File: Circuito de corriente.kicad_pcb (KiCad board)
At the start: 2 copper layers, 150 x 120 mm, 110 parts, among them J1 SALIDAS, J2 ENTRADAS, J3 +12V2, J4 +3V3, J5 +/- 5V, J6 +/- 12V, J7 INPUT_CEDCp, K1 JJM1-12V, K2 JJM1-12V, K3 JJM1-12V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

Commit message: Added 3D model
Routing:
- added copper zone on F.Cu, net GND
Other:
- board text added: "4 PINES DE ENTRADAS"

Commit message: Gerbers files generated
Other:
- board text removed: "4 PINES DE ENTRADAS"
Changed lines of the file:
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@@
       (outputformat 1)
       (mirror false)
-      (drillshape 1)
+      (drillshape 0)
       (scaleselection 1)
-      (outputdirectory "")
+      (outputdirectory "Gerbers/")
     )
   )
@@
     (effects (font (size 1 1) (thickness 0.25)))
   )
-  (gr_text "4 PINES DE ENTRADAS" (at 228.6 67.5) (layer "F.SilkS")
-    (effects (font (size 1 1) (thickness 0.15)))
-  )
   (dimension (type aligned) (layer "Margin")

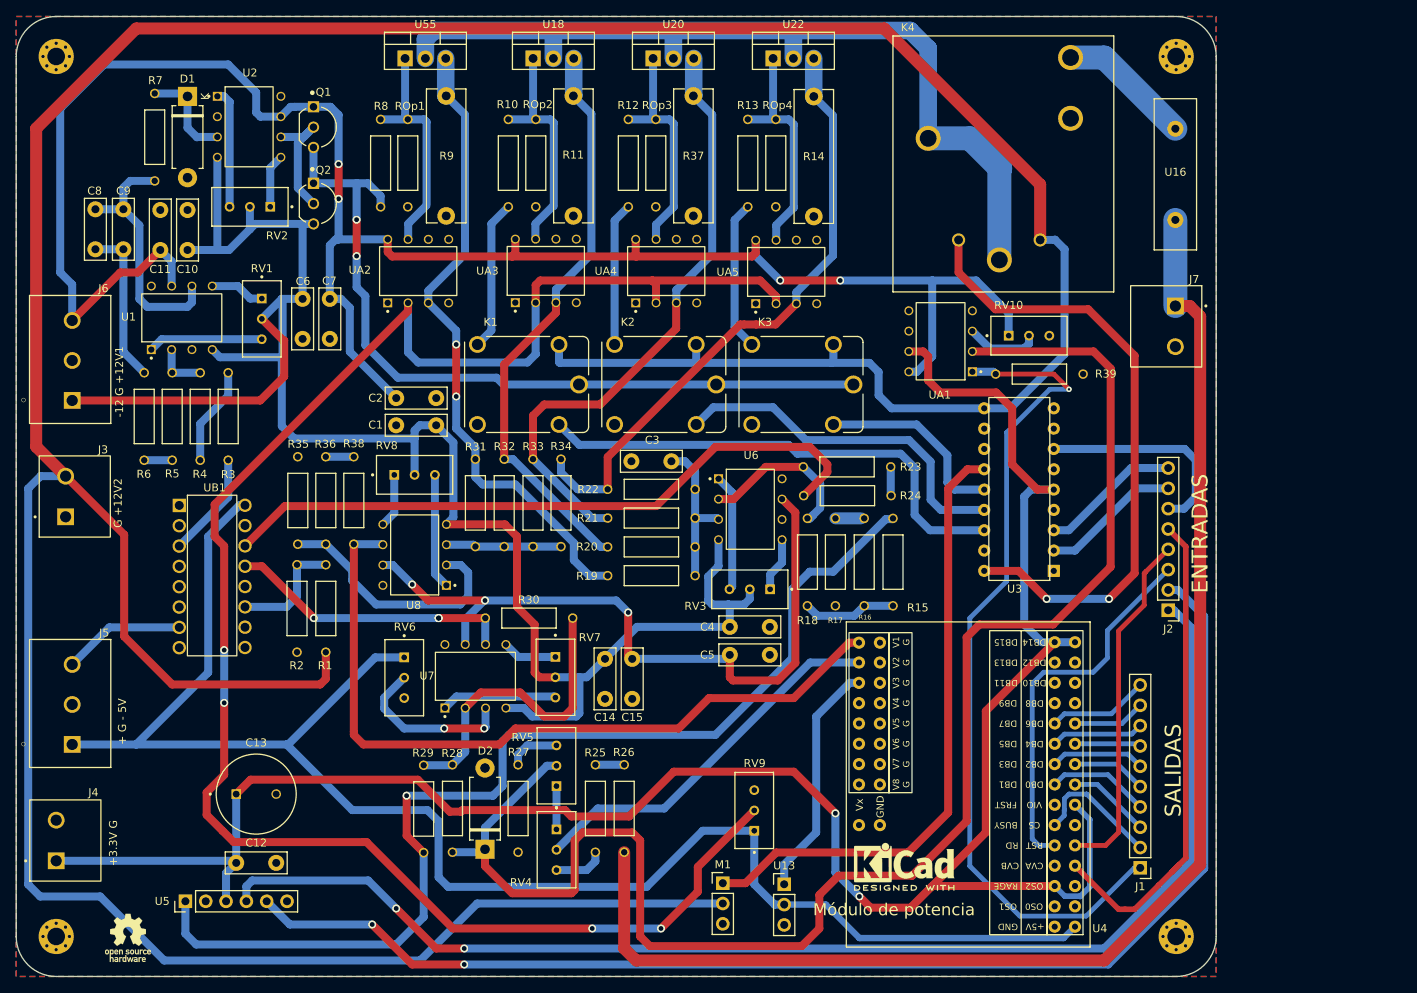
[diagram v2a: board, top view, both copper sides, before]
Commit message: Reorder conection with control module
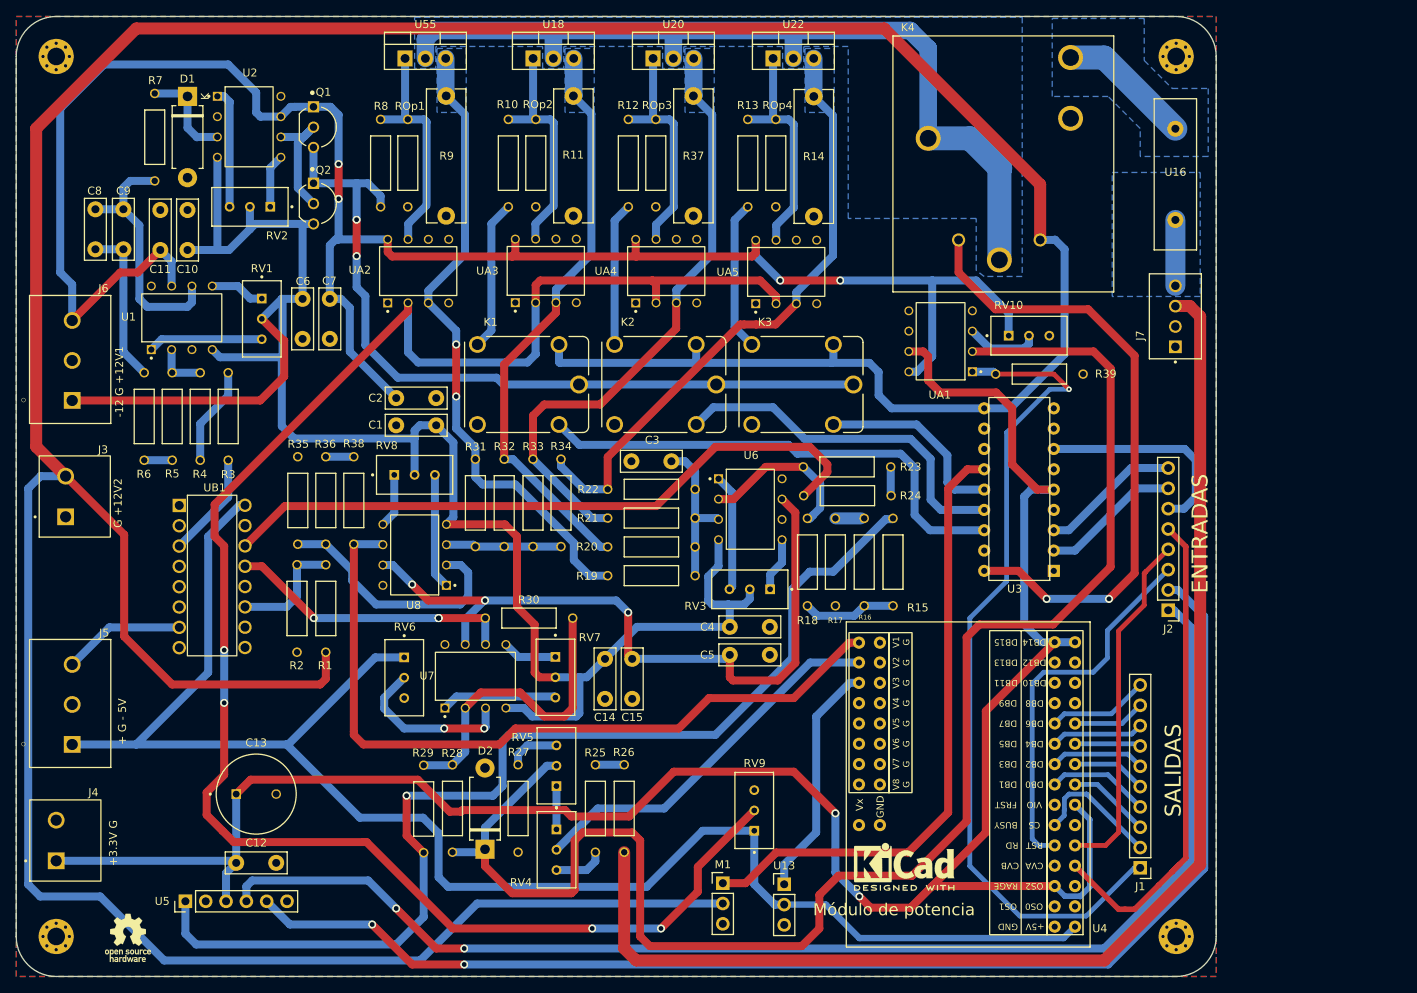
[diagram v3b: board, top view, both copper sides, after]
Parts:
- J7: footprint CEDCp:Bornera_1x2 -> CEDCp:Bornera_1x4
- moved J7 2.56 mm to (210.1, 69.0), turned to 90 degrees
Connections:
- net Net-(K4-PadNC) renamed /Proteccion Sobre Tension (53V)/F_In
- J1 pad 1: /toMicroC_OverVoltageSignal -> /toMicroC_ADC_DB0
- J1 pad 10: /toMicroC_ADC_DB7 -> /toMicroC_ADC_BUSY
- J1 pad 2: /toMicroC_ADC_BUSY -> /toMicroC_ADC_DB1
- J1 pad 3: /toMicroC_ADC_DB0 -> /toMicroC_ADC_DB2
- J1 pad 4: /toMicroC_ADC_DB1 -> /toMicroC_ADC_DB3
- J1 pad 5: /toMicroC_ADC_DB2 -> /toMicroC_ADC_DB4
- J1 pad 6: /toMicroC_ADC_DB3 -> /toMicroC_ADC_DB5
- J1 pad 7: /toMicroC_ADC_DB4 -> /toMicroC_ADC_DB6
- J1 pad 8: /toMicroC_ADC_DB5 -> /toMicroC_ADC_DB7
- J1 pad 9: /toMicroC_ADC_DB6 -> /toMicroC_OverVoltageSignal
- J2 pad 1: /fromMicroC_DACI2C_SDA -> /fromMicroC_ADC_RD
- J2 pad 2: /fromMicroC_DACI2C_SCL -> /fromMicroC_ADC_RST
- J2 pad 3: /fromMicroC_ADC_RD -> /fromMicroC_ADC_CONV
- J2 pad 4: /fromMicroC_ADC_RST -> /fromMicroC_DACI2C_SCL
- J2 pad 5: /fromMicroC_ADC_CONV -> /fromMicroC_DACI2C_SDA
- J7 pad 2: /CEP_Input+ -> GND
- K4 pad NO: unconnected-(K4-PadNO) -> GND
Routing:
- net /fromMicroC_DACI2C_SCL: track 162.8 -> 0.00 mm, vias 2 -> 0
- net /fromMicroC_ADC_RST: track 44.1 -> 206.9 mm, vias 0 -> 2
- net /fromMicroC_DACI2C_SDA: track 161.4 -> 0.00 mm, vias 2 -> 0
- net /fromMicroC_ADC_RD: track 47.5 -> 161.4 mm, vias 0 -> 2
- net /fromMicroC_ADC_CONV: track 62.1 -> 109.6 mm
- net /toMicroC_ADC_BUSY: track 16.3 -> 0.00 mm
- net /toMicroC_ADC_DB7: track 12.7 -> 24.3 mm
- net /toMicroC_ADC_DB2: track 9.31 -> 0.00 mm
- net /toMicroC_OverVoltageSignal: track 105.5 -> 114.6 mm
- net /toMicroC_ADC_DB1: track 12.9 -> 16.3 mm
- net /CEP_Input+: track 172.5 -> 170.0 mm
- net /toMicroC_ADC_DB4: track 8.26 -> 9.31 mm
- net /toMicroC_ADC_DB3: track 11.8 -> 12.9 mm
- net /+5V: track 204.9 -> 204.1 mm
- net /toMicroC_ADC_DB6: track 9.09 -> 8.26 mm
- added copper zone on B.Cu, net /CEP_Input+
- added copper zone on B.Cu, net /CEP_Input+_MOS
- added copper zone on B.Cu, net /Proteccion Sobre Tension (53V)/F_In
- added copper zone on B.Cu, net /V1
- added copper zone on B.Cu, net /V2
- added copper zone on B.Cu, net /V3
- added copper zone on B.Cu, net /V4

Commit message: Gerbers generated again
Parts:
- moved U5 118.1 mm to (199.2, 103.6), turned to -90 degrees
- moved C12 117.4 mm to (209.2, 119.2), turned to 180 degrees
- moved C13 111.6 mm to (206.7, 126.1), turned to 180 degrees
- moved M1 79.3 mm to (209.3, 79.6)
- moved REF** 77.6 mm to (98.7, 138.0)
- moved R29 71.9 mm to (187.6, 134.7), turned to 180 degrees
- moved J1 71.0 mm to (140.6, 105.8), turned to -90 degrees
- moved D2 69.0 mm to (192.7, 127.0), turned to 180 degrees
- moved R28 68.0 mm to (187.6, 131.1), turned to 180 degrees
- moved U13 68.0 mm to (94.2, 124.7)
- moved RV6 65.2 mm to (173.1, 137.2), turned to 0 degrees
- moved RV9 63.8 mm to (94.2, 118.2), turned to 180 degrees
- moved RV4 61.6 mm to (192.7, 118.1), turned to 0 degrees
- moved R27 59.7 mm to (187.6, 122.9), turned to 0 degrees
- moved U4 54.7 mm to (150.1, 114.2), turned to -90 degrees
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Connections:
- J7 pad 3: /CEP_Input+ -> /CEP_Input+_2
- J7 pad 4: /CEP_Input+ -> /CEP_Inpunt+_1
- R25 pad 1: /CEP_Input+ -> /CEP_Input+_2
- U16 pad 1: /CEP_Input+ -> /CEP_Inpunt+_1
- U2 pad 2: unconnected-(U2-Pad2) -> /PushPullOut
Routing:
- net /+12V2: track 487.2 -> 237.2 mm
- net /CEP_Input+: track 170.0 -> 0.00 mm
- net /fromMicroC_ADC_RST: track 206.9 -> 51.4 mm, vias 2 -> 0
- net /fromMicroC_ADC_RD: track 161.4 -> 54.1 mm, vias 2 -> 0
- net /+12V1: track 333.6 -> 401.2 mm, vias 7 -> 2
- net /Error2: track 36.0 -> 101.6 mm, vias 3 -> 1
- net /CEP_Input+_2: track 0.00 -> 63.1 mm
- net /fromDAC_Vref: track 135.3 -> 73.2 mm
- net /fromA6841_toFanEnable: track 77.8 -> 16.5 mm
- net /+3.3V: track 268.4 -> 329.4 mm, vias 2 -> 0
- net /toADC_LoadVoltage: track 47.5 -> 106.4 mm, vias 0 -> 2
- net /fromMicroC_ADC_CONV: track 109.6 -> 51.3 mm
- net /VI_3.3V: track 199.0 -> 146.5 mm, vias 0 -> 1
- net /ILimit_Vref: track 224.5 -> 185.6 mm, vias 4 -> 0
- net /PushPullOut: track 98.6 -> 135.0 mm, vias 2 -> 0
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- added copper zone on B.Cu, net /CEP_Inpunt+_1
- removed copper zone on B.Cu, net /CEP_Input+

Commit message: Version V1 (Clearence + pads)
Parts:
- C13: value 1u -> 10u
- D1: value 1N47xxA -> BZX384B3V9
- R2: value 2k7 -> 1k2
- UB1: value 74HC4051N,652 -> 74HC4051N
- moved Q2 0.08 mm to (103.7, 49.6)
- moved R19 0.06 mm to (144.5, 97.7)
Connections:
- U4 pad 27: GND -> /fromMicroC_ADC_CONV
- U5 pad 2: unconnected-(U5-Pad2) -> GND
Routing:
- net /Error1: track 82.2 -> 118.3 mm
- net /-12V: track 208.4 -> 235.9 mm
- net /+12V1: track 401.2 -> 416.2 mm
- net /fromMicroC_A6841ST1: track 12.2 -> 26.3 mm
- net Net-(R31-Pad2): track 18.7 -> 31.9 mm
- net Net-(C3-Pad2): track 19.9 -> 29.7 mm
- net /+5V: track 212.0 -> 220.4 mm
- net /Circuito de control de corriente/GS1: track 27.4 -> 35.6 mm
- net /fromA6841_PowerEnable: track 54.6 -> 62.7 mm, vias 0 -> 2
- net /+3.3V: track 329.4 -> 337.4 mm
- net /V1: track 83.1 -> 90.5 mm
- net Net-(RV1-Pad1): track 7.19 -> 14.4 mm
- net Net-(R28-Pad2): track 28.8 -> 35.0 mm
- net /toADC_MOSFETsTemp: track 33.3 -> 39.1 mm
- net Net-(R18-Pad2): track 29.8 -> 24.0 mm
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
